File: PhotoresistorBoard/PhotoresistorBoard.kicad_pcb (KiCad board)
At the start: 2 copper layers, 17.8 x 20.3 mm, 7 parts, among them J1 CONN_01X03

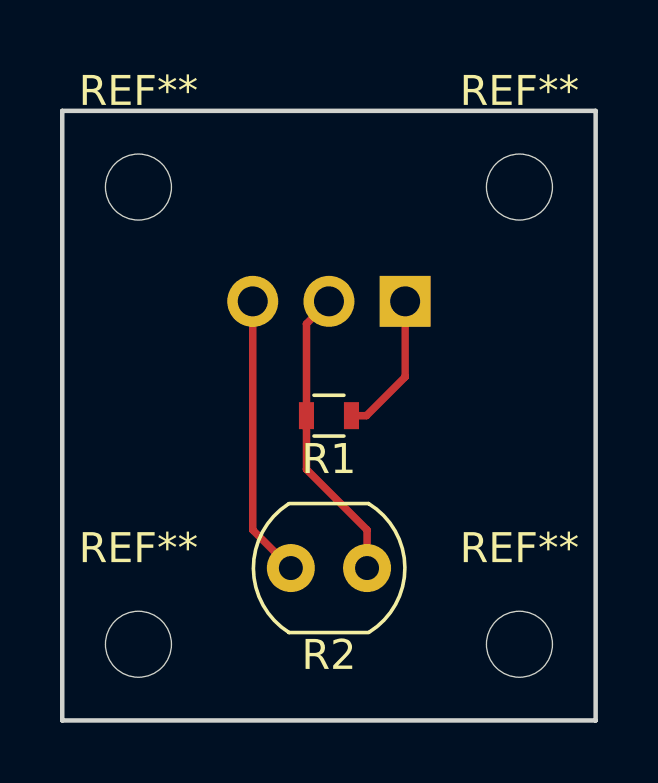
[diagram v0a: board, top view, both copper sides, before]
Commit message: Added WhiteLEDboard
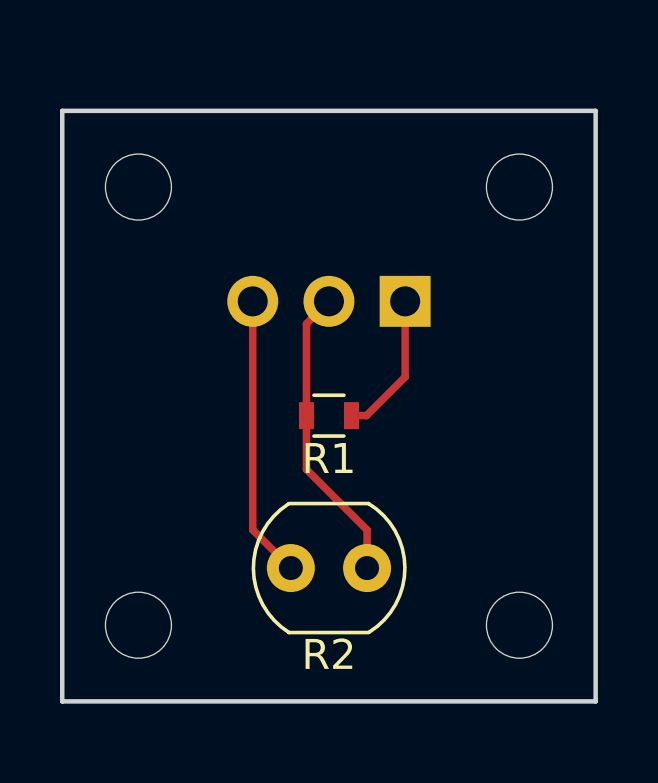
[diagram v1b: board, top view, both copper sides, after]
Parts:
- moved REF** 0.63 mm to (142.2, 104.8)
- moved REF** 0.63 mm to (154.9, 104.8)
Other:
- board size 17.8 x 20.3 mm -> 17.8 x 19.7 mm
- board text added: "Hydrosense"
- board text added: "Photoresistor"
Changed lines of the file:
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@@
 (kicad_pcb (version 4) (host pcbnew 4.0.6-e0-6349~53~ubuntu16.04.1)
   (general
-    (links 0)
-    (no_connects 4)
-    (area 139.624999 87.554999 157.555001 108.025001)
+    (links 4)
+    (no_connects 0)
+    (area 139.624999 87.554999 157.555001 107.390001)
     (thickness 1.6)
-    (drawings 4)
+    (drawings 6)
     (tracks 10)
     (zones 0)
@@
     (descr "Through hole angled pin header, 1x03, 2.54mm pitch, 6mm pin length, single row")
     (tags "Through hole angled pin header THT 1x03 2.54mm single row")
-    (fp_text reference J1 (at 4.315 2.27 90) (layer B.SilkS)
+    (fp_text reference J1 (at 4.315 2.27 90) (layer B.SilkS) hide
       (effects (font (size 1 1) (thickness 0.15)) (justify mirror))
     )
-    (fp_text value CONN_01X03 (at 4.315 -7.35 90) (layer B.Fab)
+    (fp_text value CONN_01X03 (at 4.315 -7.35 90) (layer B.Fab) hide
       (effects (font (size 1 1) (thickness 0.15)) (justify mirror))
     )
@@
     (descr "Mounting Hole 2.2mm, no annular, M2")
     (tags "mounting hole 2.2mm no annular m2")
-    (fp_text reference REF** (at 0 -3.2) (layer F.SilkS)
-      (effects (font (size 1 1) (thickness 0.15)))
-    )
-    (fp_text value MountingHole_2.2mm_M2 (at 0 3.2) (layer F.Fab)
+    (fp_text reference REF** (at 0 -3.2) (layer F.SilkS) hide
+      (effects (font (size 1 1) (thickness 0.15)))
+    )
+    (fp_text value MountingHole_2.2mm_M2 (at 0 3.2) (layer F.Fab) hide
       (effects (font (size 1 1) (thickness 0.15)))
     )
@@
     (descr "Mounting Hole 2.2mm, no annular, M2")
     (tags "mounting hole 2.2mm no annular m2")
-    (fp_text reference REF** (at 0 -3.2) (layer F.SilkS)
-      (effects (font (size 1 1) (thickness 0.15)))
-    )
-    (fp_text value MountingHole_2.2mm_M2 (at 0 3.2) (layer F.Fab)
+    (fp_text reference REF** (at 0 -3.2) (layer F.SilkS) hide
+      (effects (font (size 1 1) (thickness 0.15)))
+    )
+    (fp_text value MountingHole_2.2mm_M2 (at 0 3.2) (layer F.Fab) hide
       (effects (font (size 1 1) (thickness 0.15)))
     )
@@
   )
   (module Mounting_Holes:MountingHole_2.2mm_M2 (layer F.Cu)
-    (at 142.24 105.41)
+    (at 142.24 104.775)
     (descr "Mounting Hole 2.2mm, no annular, M2")
     (tags "mounting hole 2.2mm no annular m2")
-    (fp_text reference REF** (at 0 -3.2) (layer F.SilkS)
-      (effects (font (size 1 1) (thickness 0.15)))
-    )
-    (fp_text value MountingHole_2.2mm_M2 (at 0 3.2) (layer F.Fab)
+    (fp_text reference REF** (at 0 -3.2) (layer F.SilkS) hide
+      (effects (font (size 1 1) (thickness 0.15)))
+    )
+    (fp_text value MountingHole_2.2mm_M2 (at 0 3.2) (layer F.Fab) hide
       (effects (font (size 1 1) (thickness 0.15)))
     )
@@
   )
   (module Mounting_Holes:MountingHole_2.2mm_M2 (layer F.Cu)
-    (at 154.94 105.41)
+    (at 154.94 104.775)
     (descr "Mounting Hole 2.2mm, no annular, M2")
     (tags "mounting hole 2.2mm no annular m2")
-    (fp_text reference REF** (at 0 -3.2) (layer F.SilkS)
-      (effects (font (size 1 1) (thickness 0.15)))
-    )
-    (fp_text value MountingHole_2.2mm_M2 (at 0 3.2) (layer F.Fab)
+    (fp_text reference REF** (at 0 -3.2) (layer F.SilkS) hide
+      (effects (font (size 1 1) (thickness 0.15)))
+    )
+    (fp_text value MountingHole_2.2mm_M2 (at 0 3.2) (layer F.Fab) hide
       (effects (font (size 1 1) (thickness 0.15)))
     )
@@
     (pad 1 np_thru_hole circle (at 0 0) (size 2.2 2.2) (drill 2.2) (layers *.Cu *.Mask))
   )
-  (gr_line (start 139.7 107.95) (end 139.7 87.63) (layer Edge.Cuts) (width 0.15))
-  (gr_line (start 157.48 107.95) (end 139.7 107.95) (layer Edge.Cuts) (width 0.15))
-  (gr_line (start 157.48 87.63) (end 157.48 107.95) (layer Edge.Cuts) (width 0.15))
+  (gr_text Photoresistor (at 148.59 99.695) (layer B.SilkS)
+    (effects (font (size 1 1) (thickness 0.25)) (justify mirror))
+  )
+  (gr_text Hydrosense (at 148.59 97.155) (layer B.SilkS)
+    (effects (font (size 1.5 1.5) (thickness 0.3)) (justify mirror))
+  )
+  (gr_line (start 157.48 87.63) (end 157.48 107.315) (layer Edge.Cuts) (width 0.15))
+  (gr_line (start 139.7 87.63) (end 139.7 107.315) (layer Edge.Cuts) (width 0.15))
+  (gr_line (start 157.48 107.315) (end 139.7 107.315) (layer Edge.Cuts) (width 0.15))
   (gr_line (start 139.7 87.63) (end 157.48 87.63) (layer Edge.Cuts) (width 0.15))
   (segment (start 151.13 93.98) (end 151.13 96.5) (width 0.25) (layer F.Cu) (net 1))
